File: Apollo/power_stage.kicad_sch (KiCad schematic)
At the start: 14 parts, among them T1 Transformer_SP_1S, T2 Transformer_SP_1S, U1 EL84, U2 EL84

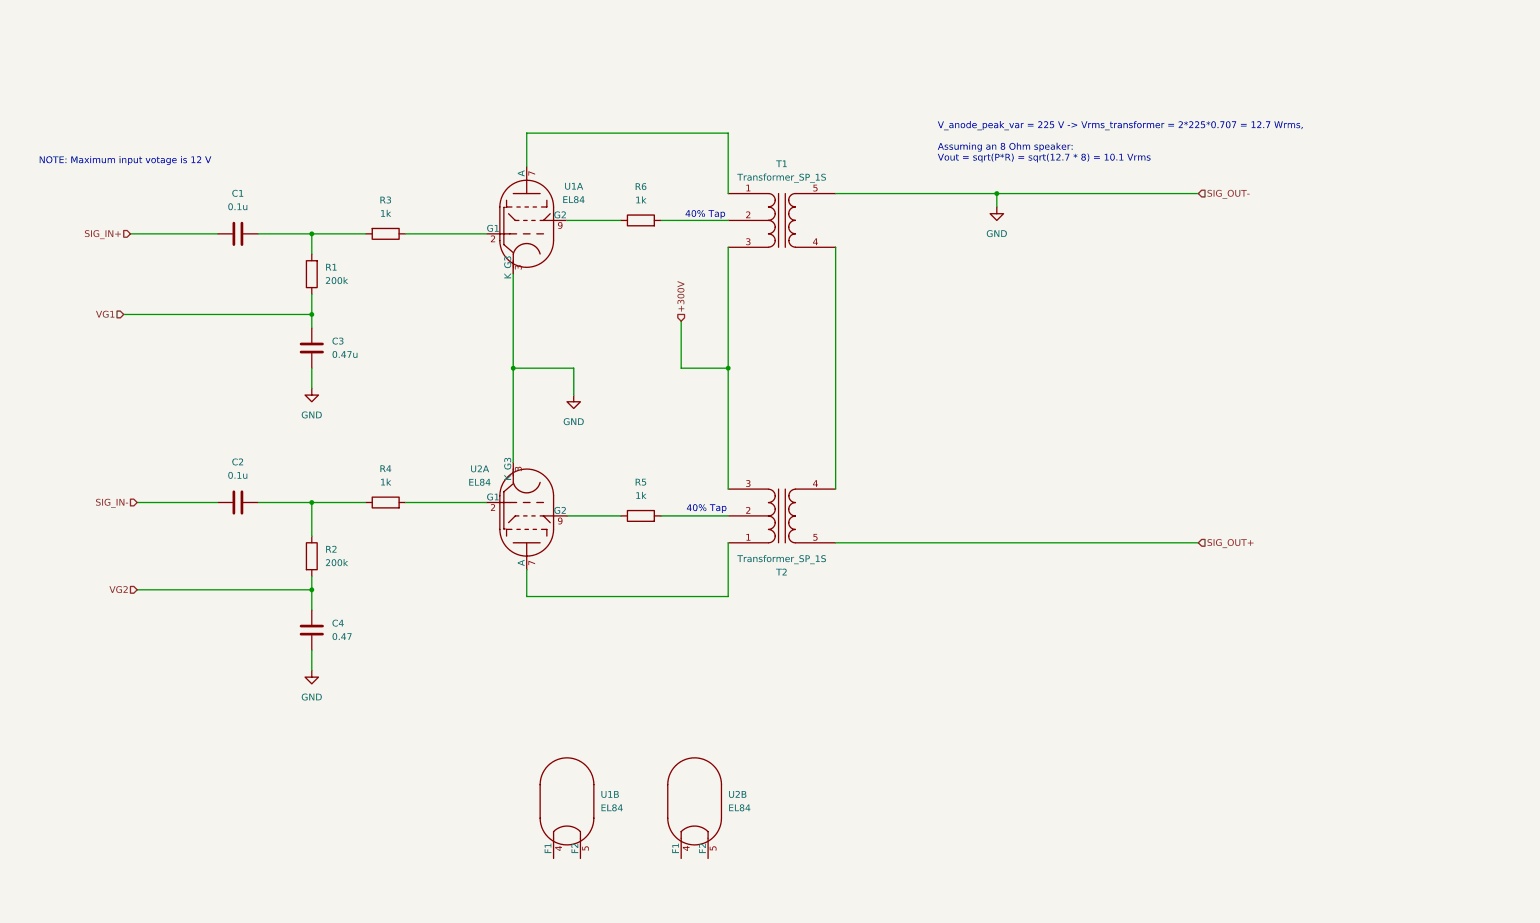
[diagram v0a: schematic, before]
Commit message: Add comments to power stage
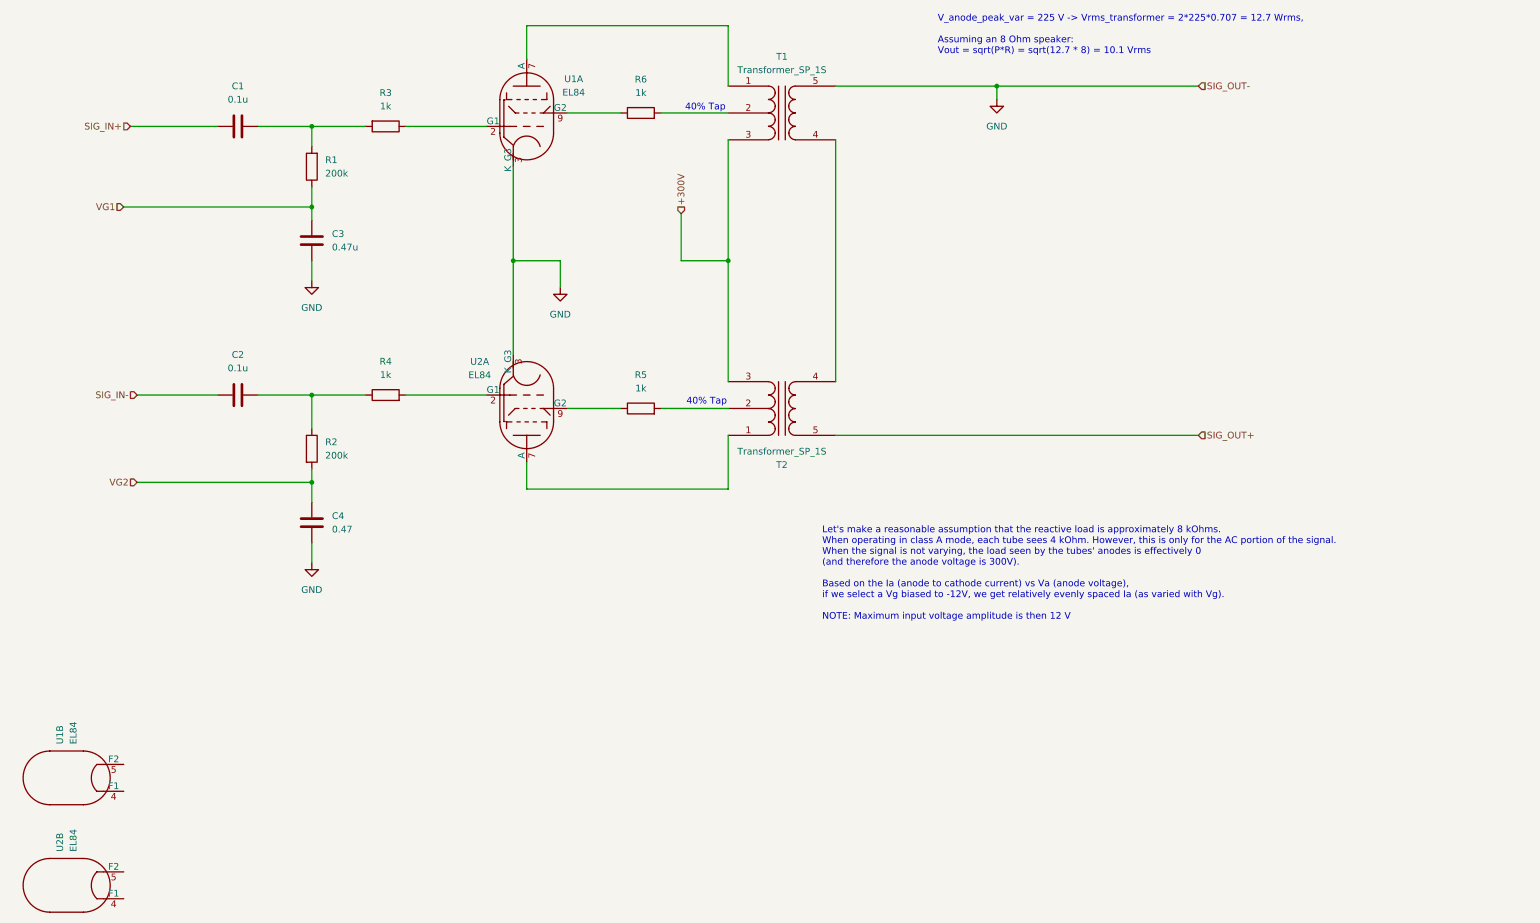
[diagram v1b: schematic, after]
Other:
- note added: "Let's make a reasonable assumption that the reactive load is approximately 8 kOhms. When operating in class A mode, each tube sees 4 kOhm. However, this is only for the AC portion of the signal. When the signal is not varying, the load seen by the tubes' anodes is effectively 0 (and therefore the anode voltage is 300V). Based on the Ia (anode to cathode current) vs Va (anode voltage), if we selec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"
- note removed: "NOTE: Maximum input votage is 12 V"
- moved on the sheet: C1, C2, C3, C4, R1, R2, R3, R4, R5, R6, T1, T2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
